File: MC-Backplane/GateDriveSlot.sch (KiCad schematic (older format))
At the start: 1 part, among them U6 86094328314755V1LF

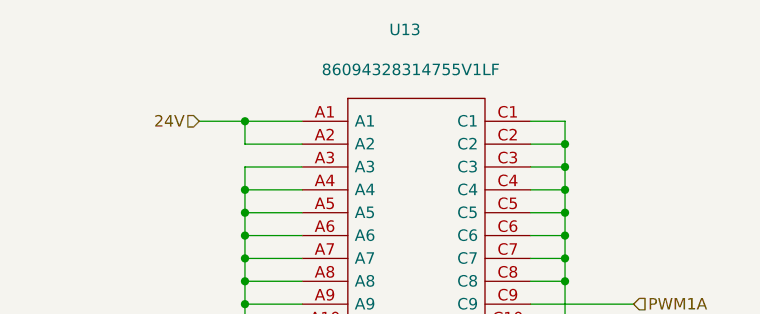
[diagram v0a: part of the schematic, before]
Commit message: placement done- tracks started
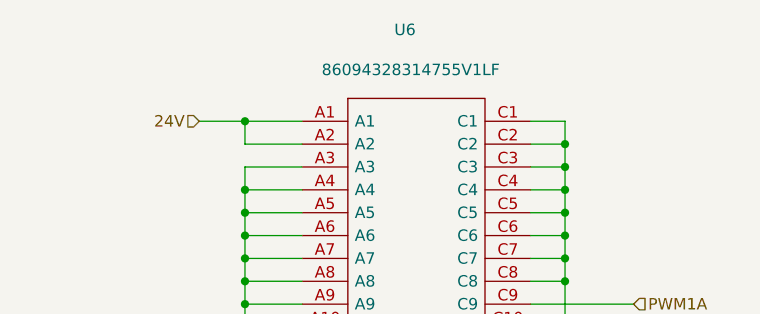
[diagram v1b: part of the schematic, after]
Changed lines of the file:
@@
 $Descr A4 11693 8268
 encoding utf-8
-Sheet 13 14
+Sheet 6 14
 Title ""
 Date ""
@@
 AR Path="/6245C75C/6229BF81" Ref="U8"  Part="1"
 AR Path="/6245C76A/6229BF81" Ref="U9"  Part="1"
-F 0 "U13" H 5375 2900 50  0000 C CNN
+F 0 "U6" H 5375 2900 50  0000 C CNN
 F 1 "86094328314755V1LF" H 5400 2725 50  0000 C CNN
 F 2 "Footprints_MC-Backplane:86094328314755V1LF" H 4925 2500 50  0001 C CNN

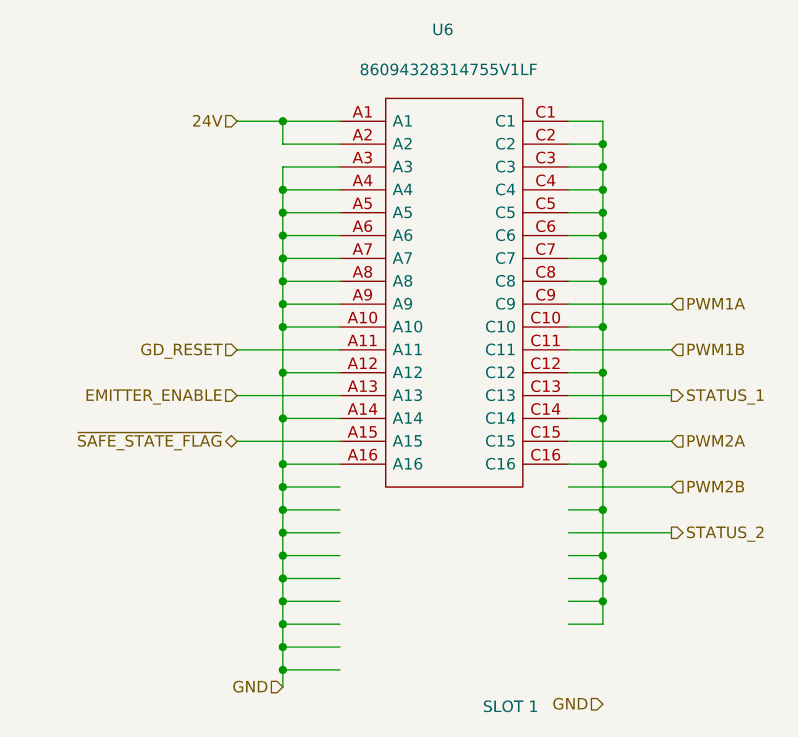
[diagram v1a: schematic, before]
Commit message: layout done: cleaning up and checking MH
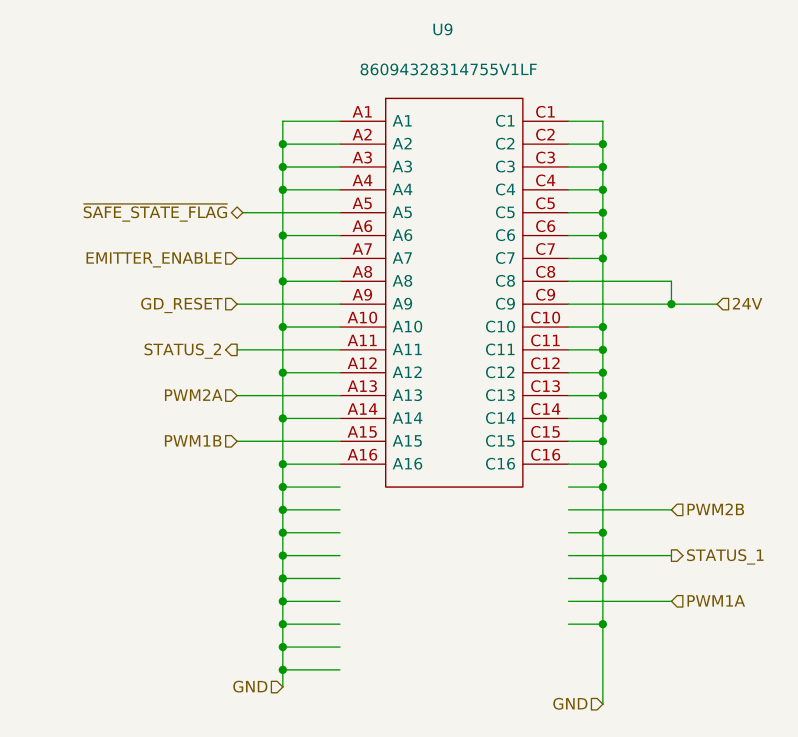
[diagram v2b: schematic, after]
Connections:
- wire segments 86 -> 87
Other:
- note removed: "SLOT 1"
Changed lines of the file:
@@
 $Descr A4 11693 8268
 encoding utf-8
-Sheet 6 14
+Sheet 9 14
 Title ""
 Date ""
@@
 AR Path="/6245C75C/6229BF81" Ref="U8"  Part="1"
 AR Path="/6245C76A/6229BF81" Ref="U9"  Part="1"
-F 0 "U6" H 5375 2900 50  0000 C CNN
+F 0 "U9" H 5375 2900 50  0000 C CNN
 F 1 "86094328314755V1LF" H 5400 2725 50  0000 C CNN
 F 2 "Footprints_MC-Backplane:86094328314755V1LF" H 4925 2500 50  0001 C CNN
@@
 $EndComp
 Wire Wire Line
-	5925 3300 6375 3300
-Wire Wire Line
 	5925 3400 6075 3400
-Wire Wire Line
-	6075 3400 6075 3600
-Wire Wire Line
-	6075 3400 6075 3200
-Wire Wire Line
-	6075 3200 5925 3200
 Connection ~ 6075 3400
 Wire Wire Line
-	5925 3600 6075 3600
-Connection ~ 6075 3600
-Wire Wire Line
-	6075 3600 6075 3800
-Wire Wire Line
-	5925 3800 6075 3800
-Connection ~ 6075 3800
-Wire Wire Line
-	6075 3800 6075 4000
-Wire Wire Line
-	5925 4000 6075 4000
-Connection ~ 6075 4000
-Wire Wire Line
-	6075 4000 6075 4200
-Wire Wire Line
-	5925 4200 6075 4200
-Connection ~ 6075 4200
-Wire Wire Line
-	6075 4200 6075 4400
-Wire Wire Line
-	5925 4400 6075 4400
-Connection ~ 6075 4400
-Wire Wire Line
-	6075 4400 6075 4500
-Wire Wire Line
-	5925 4600 6075 4600
-Wire Wire Line
-	4925 2700 4675 2700
-Wire Wire Line
-	4925 2900 4675 2900
-Connection ~ 4675 2900
-Wire Wire Line
-	4925 3100 4675 3100
-Connection ~ 4675 3100
-Wire Wire Line
-	4675 3100 4675 3200
+	4925 2500 4675 2500
 Wire Wire Line
 	4925 3200 4675 3200
 Connection ~ 4675 3200
 Wire Wire Line
-	4675 3200 4675 3300
-Wire Wire Line
-	4925 3300 4675 3300
-Connection ~ 4675 3300
-Wire Wire Line
-	4675 3300 4675 3400
-Wire Wire Line
 	4925 3400 4675 3400
-Text Notes 5550 5100 0    50   ~ 0
-SLOT 1
 Text HLabel 6075 5050 0    50   Input ~ 0
 GND
 Wire Wire Line
-	5925 3700 6375 3700
-Wire Wire Line
-	5925 3500 6375 3500
-Wire Wire Line
-	5925 4300 6375 4300
-Wire Wire Line
-	5925 3900 6375 3900
-Wire Wire Line
-	5925 4100 6375 4100
-Wire Wire Line
-	5925 4500 6075 4500
-Text HLabel 4475 2500 0    50   Input ~ 0
+	5925 4400 6375 4400
+Wire Wire Line
+	5925 4600 6375 4600
+Text HLabel 6575 3300 2    50   Input ~ 0
 24V
 Wire Wire Line
-	4675 2700 4675 2800
-Wire Wire Line
-	4675 2900 4675 3000
-Text HLabel 4475 3700 0    50   Input ~ 0
-EMITTER_ENABLE
-Wire Wire Line
-	4925 3900 4475 3900
-Wire Wire Line
-	4475 3700 4925 3700
-Wire Wire Line
-	4475 3500 4925 3500
+	4925 3700 4475 3700
+Wire Wire Line
+	5925 4200 6375 4200
+Wire Wire Line
+	4475 3900 4925 3900
 Wire Wire Line
 	4925 3600 4675 3600
-Wire Wire Line
-	4675 3600 4675 3800
-Wire Wire Line
-	4925 3800 4675 3800
-Connection ~ 4675 3800
 Wire Wire Line
 	4675 3400 4675 3600
 Connection ~ 4675 3400
-Connection ~ 4675 3600
-Connection ~ 6075 4500
-Wire Wire Line
-	6075 4500 6075 4600
-Wire Wire Line
-	4925 2800 4675 2800
-Connection ~ 4675 2800
-Wire Wire Line
-	4675 2800 4675 2900
+Wire Wire Line
+	4925 2600 4675 2600
 Wire Wire Line
 	4925 3000 4675 3000
 Connection ~ 4675 3000
 Wire Wire Line
-	4675 3000 4675 3100
-Wire Wire Line
-	4675 3800 4675 4000
-Wire Wire Line
-	4925 4000 4675 4000
-Connection ~ 4675 4000
-Wire Wire Line
-	4675 4000 4675 4100
-Wire Wire Line
-	4475 2500 4675 2500
-Wire Wire Line
-	4675 2600 4675 2500
-Wire Wire Line
-	4675 2600 4925 2600
-Connection ~ 4675 2500
-Wire Wire Line
-	4675 2500 4925 2500
-Wire Wire Line
-	5925 4700 6075 4700
+	6575 3300 6375 3300
+Wire Wire Line
+	6375 3200 6375 3300
+Wire Wire Line
+	6375 3200 5925 3200
+Connection ~ 6375 3300
+Wire Wire Line
+	6375 3300 5925 3300
 Wire Wire Line
 	4925 4100 4675 4100
-Connection ~ 4675 4100
 Wire Wire Line
 	4925 4200 4675 4200
@@
 Connection ~ 4675 4900
 Wire Wire Line
-	6075 3200 6075 3100
-Wire Wire Line
 	6075 2500 5925 2500
-Connection ~ 6075 3200
 Wire Wire Line
 	5925 2600 6075 2600
@@
 Wire Wire Line
 	6075 3100 6075 3000
-Text HLabel 4475 3900 0    50   BiDi ~ 0
+Text HLabel 6375 4600 2    50   Input ~ 0
+PWM1A
+Text HLabel 6375 4200 2    50   Input ~ 0
+PWM2B
+Text HLabel 4475 3700 0    50   Input ~ 0
+PWM2A
+Text HLabel 4475 3500 0    50   Output ~ 0
+STATUS_2
+Text HLabel 4475 3900 0    50   Input ~ 0
+PWM1B
+Text HLabel 6375 4400 2    50   Output ~ 0
+STATUS_1
+Text HLabel 4475 3300 0    50   Input ~ 0
+GD_RESET
+Text HLabel 4500 2900 0    50   BiDi ~ 0
 ~SAFE_STATE_FLAG~
-Text HLabel 4475 3500 0    50   Input ~ 0
-GD_RESET
-Text HLabel 6375 3700 2    50   Output ~ 0
-STATUS_1
-Text HLabel 6375 3500 2    50   Input ~ 0
-PWM1B
-Text HLabel 6375 4300 2    50   Output ~ 0
-STATUS_2
-Text HLabel 6375 3900 2    50   Input ~ 0
-PWM2A
-Text HLabel 6375 4100 2    50   Input ~ 0
-PWM2B
-Text HLabel 6375 3300 2    50   Input ~ 0
-PWM1A
-Wire Wire Line
-	6075 4600 6075 4700
-Connection ~ 6075 4600
+Text HLabel 4475 3100 0    50   Input ~ 0
+EMITTER_ENABLE
+Wire Wire Line
+	6075 3400 6075 3500
+Wire Wire Line
+	4925 2800 4675 2800
+Connection ~ 4675 2800
+Wire Wire Line
+	4675 3200 4675 3400
+Wire Wire Line
+	4475 3500 4925 3500
+Wire Wire Line
+	4675 3800 4675 4000
+Connection ~ 4675 4100
+Wire Wire Line
+	4675 3600 4675 3800
+Connection ~ 4675 3600
+Connection ~ 4675 3800
+Wire Wire Line
+	4675 3800 4925 3800
+Wire Wire Line
+	4675 2600 4675 2500
+Connection ~ 4675 2600
+Wire Wire Line
+	4675 2600 4675 2700
+Wire Wire Line
+	4925 3100 4475 3100
+Wire Wire Line
+	4925 3300 4475 3300
+Wire Wire Line
+	5925 3500 6075 3500
+Connection ~ 6075 3500
+Wire Wire Line
+	5925 3600 6075 3600
+Wire Wire Line
+	5925 3700 6075 3700
+Wire Wire Line
+	5925 3800 6075 3800
+Wire Wire Line
+	5925 3900 6075 3900
+Connection ~ 6075 3900
+Wire Wire Line
+	6075 3900 6075 4000
+Wire Wire Line
+	5925 4100 6075 4100
+Connection ~ 6075 4100
+Wire Wire Line
+	6075 4100 6075 4300
+Wire Wire Line
+	5925 4300 6075 4300
+Connection ~ 6075 4300
+Wire Wire Line
+	5925 4500 6075 4500
+Wire Wire Line
+	6075 4300 6075 4500
+Connection ~ 6075 4500
+Wire Wire Line
+	5925 4700 6075 4700
+Connection ~ 6075 4700
+Wire Wire Line
+	6075 4700 6075 5050
+Wire Wire Line
+	6075 3500 6075 3600
+Connection ~ 6075 3600
+Wire Wire Line
+	6075 3600 6075 3700
+Connection ~ 6075 3700
+Wire Wire Line
+	6075 3700 6075 3800
+Connection ~ 6075 3800
+Wire Wire Line
+	6075 3800 6075 3900
+Wire Wire Line
+	4675 3000 4675 3200
+Wire Wire Line
+	4675 2800 4675 3000
+Wire Wire Line
+	4925 2900 4500 2900
+Wire Wire Line
+	4925 2700 4675 2700
+Connection ~ 4675 2700
+Wire Wire Line
+	4675 2700 4675 2800
+Wire Wire Line
+	6075 3100 6075 3400
+Wire Wire Line
+	6075 4500 6075 4700
+Wire Wire Line
+	5925 4000 6075 4000
+Connection ~ 6075 4000
+Wire Wire Line
+	6075 4000 6075 4100
+Wire Wire Line
+	4925 4000 4675 4000
+Connection ~ 4675 4000
+Wire Wire Line
+	4675 4000 4675 4100
 $EndSCHEMATC

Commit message: Layout ready for review
- double check measurements and connector placement
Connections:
- wire segments 87 -> 55
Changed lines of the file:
@@
 $Descr A4 11693 8268
 encoding utf-8
-Sheet 9 14
+Sheet 6 14
 Title ""
 Date ""
@@
 Comment4 ""
 $EndDescr
+Wire Wire Line
+	4925 2500 4675 2500
+Wire Wire Line
+	4925 3200 4675 3200
+Connection ~ 4675 3200
+Wire Wire Line
+	4925 3400 4675 3400
+Text HLabel 6075 4350 0    50   Input ~ 0
+GND
+Wire Wire Line
+	5925 3700 6375 3700
+Wire Wire Line
+	5925 3900 6375 3900
+Text HLabel 6575 2600 2    50   Input ~ 0
+24V
+Wire Wire Line
+	4925 3700 4475 3700
+Wire Wire Line
+	5925 3500 6375 3500
+Wire Wire Line
+	4475 3900 4925 3900
+Wire Wire Line
+	4925 3600 4675 3600
+Wire Wire Line
+	4675 3400 4675 3600
+Connection ~ 4675 3400
+Wire Wire Line
+	4925 2600 4675 2600
+Wire Wire Line
+	4925 3000 4675 3000
+Connection ~ 4675 3000
+Wire Wire Line
+	6575 2600 6375 2600
+Wire Wire Line
+	6375 2500 6375 2600
+Wire Wire Line
+	6375 2500 5925 2500
+Connection ~ 6375 2600
+Wire Wire Line
+	6375 2600 5925 2600
+Text HLabel 4675 4350 0    50   Input ~ 0
+GND
+Text HLabel 6375 3900 2    50   Input ~ 0
+PWM1A
+Text HLabel 6375 3500 2    50   Input ~ 0
+PWM2B
+Text HLabel 4475 3700 0    50   Input ~ 0
+PWM2A
+Text HLabel 4475 3500 0    50   Output ~ 0
+STATUS_2
+Text HLabel 4475 3900 0    50   Input ~ 0
+PWM1B
+Text HLabel 6375 3700 2    50   Output ~ 0
+STATUS_1
+Text HLabel 4475 3300 0    50   Input ~ 0
+GD_RESET
+Text HLabel 4500 2900 0    50   BiDi ~ 0
+~SAFE_STATE_FLAG~
+Text HLabel 4475 3100 0    50   Input ~ 0
+EMITTER_ENABLE
+Wire Wire Line
+	4925 2800 4675 2800
+Connection ~ 4675 2800
+Wire Wire Line
+	4675 3200 4675 3400
+Wire Wire Line
+	4475 3500 4925 3500
+Wire Wire Line
+	4675 3800 4675 4000
+Wire Wire Line
+	4675 3600 4675 3800
+Connection ~ 4675 3600
+Connection ~ 4675 3800
+Wire Wire Line
+	4675 3800 4925 3800
+Wire Wire Line
+	4675 2600 4675 2500
+Connection ~ 4675 2600
+Wire Wire Line
+	4675 2600 4675 2700
+Wire Wire Line
+	4925 3100 4475 3100
+Wire Wire Line
+	4925 3300 4475 3300
+Wire Wire Line
+	5925 3400 6075 3400
+Wire Wire Line
+	6075 3400 6075 3600
+Wire Wire Line
+	5925 3600 6075 3600
+Connection ~ 6075 3600
+Wire Wire Line
+	5925 3800 6075 3800
+Wire Wire Line
+	6075 3600 6075 3800
+Connection ~ 6075 3800
+Wire Wire Line
+	5925 4000 6075 4000
+Connection ~ 6075 4000
+Wire Wire Line
+	6075 4000 6075 4350
+Wire Wire Line
+	4675 3000 4675 3200
+Wire Wire Line
+	4675 2800 4675 3000
+Wire Wire Line
+	4925 2900 4500 2900
+Wire Wire Line
+	4925 2700 4675 2700
+Connection ~ 4675 2700
+Wire Wire Line
+	4675 2700 4675 2800
+Wire Wire Line
+	6075 3800 6075 4000
+Wire Wire Line
+	4925 4000 4675 4000
+Connection ~ 6075 3400
+Wire Wire Line
+	6075 3300 6075 3400
+Connection ~ 6075 3300
+Wire Wire Line
+	5925 3300 6075 3300
+Wire Wire Line
+	6075 3200 6075 3300
+Connection ~ 6075 3200
+Wire Wire Line
+	5925 3200 6075 3200
+Wire Wire Line
+	6075 3100 6075 3200
+Connection ~ 6075 3100
+Wire Wire Line
+	5925 3100 6075 3100
+Wire Wire Line
+	6075 3000 6075 3100
+Connection ~ 6075 3000
+Wire Wire Line
+	5925 3000 6075 3000
+Wire Wire Line
+	6075 2900 6075 3000
+Connection ~ 6075 2900
+Wire Wire Line
+	5925 2900 6075 2900
+Wire Wire Line
+	6075 2800 6075 2900
+Connection ~ 6075 2800
+Wire Wire Line
+	5925 2800 6075 2800
+Wire Wire Line
+	6075 2700 6075 2800
+Wire Wire Line
+	5925 2700 6075 2700
+Connection ~ 4675 4000
 $Comp
 L Existing_IC_Models:86094328314755V1LF U?
@@
 AR Path="/6245C75C/6229BF81" Ref="U8"  Part="1"
 AR Path="/6245C76A/6229BF81" Ref="U9"  Part="1"
-F 0 "U9" H 5375 2900 50  0000 C CNN
+F 0 "U6" H 5375 2900 50  0000 C CNN
 F 1 "86094328314755V1LF" H 5400 2725 50  0000 C CNN
 F 2 "Footprints_MC-Backplane:86094328314755V1LF" H 4925 2500 50  0001 C CNN
@@
 $EndComp
 Wire Wire Line
-	5925 3400 6075 3400
-Connection ~ 6075 3400
-Wire Wire Line
-	4925 2500 4675 2500
-Wire Wire Line
-	4925 3200 4675 3200
-Connection ~ 4675 3200
-Wire Wire Line
-	4925 3400 4675 3400
-Text HLabel 6075 5050 0    50   Input ~ 0
-GND
-Wire Wire Line
-	5925 4400 6375 4400
-Wire Wire Line
-	5925 4600 6375 4600
-Text HLabel 6575 3300 2    50   Input ~ 0
-24V
-Wire Wire Line
-	4925 3700 4475 3700
-Wire Wire Line
-	5925 4200 6375 4200
-Wire Wire Line
-	4475 3900 4925 3900
-Wire Wire Line
-	4925 3600 4675 3600
-Wire Wire Line
-	4675 3400 4675 3600
-Connection ~ 4675 3400
-Wire Wire Line
-	4925 2600 4675 2600
-Wire Wire Line
-	4925 3000 4675 3000
-Connection ~ 4675 3000
-Wire Wire Line
-	6575 3300 6375 3300
-Wire Wire Line
-	6375 3200 6375 3300
-Wire Wire Line
-	6375 3200 5925 3200
-Connection ~ 6375 3300
-Wire Wire Line
-	6375 3300 5925 3300
-Wire Wire Line
-	4925 4100 4675 4100
-Wire Wire Line
-	4925 4200 4675 4200
-Wire Wire Line
-	4925 4300 4675 4300
-Wire Wire Line
-	4925 4400 4675 4400
-Wire Wire Line
-	4925 4500 4675 4500
-Wire Wire Line
-	4925 4600 4675 4600
-Wire Wire Line
-	4925 4700 4675 4700
-Wire Wire Line
-	4925 4800 4675 4800
-Wire Wire Line
-	4925 4900 4675 4900
-Connection ~ 4675 4400
-Wire Wire Line
-	4675 4400 4675 4500
-Connection ~ 4675 4500
-Wire Wire Line
-	4675 4500 4675 4600
-Connection ~ 4675 4600
-Wire Wire Line
-	4675 4600 4675 4700
-Connection ~ 4675 4700
-Wire Wire Line
-	4675 4700 4675 4800
-Connection ~ 4675 4800
-Wire Wire Line
-	4675 4800 4675 4900
-Text HLabel 4675 4975 0    50   Input ~ 0
-GND
-Wire Wire Line
-	4675 4100 4675 4200
-Connection ~ 4675 4300
-Wire Wire Line
-	4675 4300 4675 4400
-Connection ~ 4675 4200
-Wire Wire Line
-	4675 4200 4675 4300
-Wire Wire Line
-	4675 4900 4675 4975
-Connection ~ 4675 4900
-Wire Wire Line
-	6075 2500 5925 2500
-Wire Wire Line
-	5925 2600 6075 2600
-Connection ~ 6075 2600
-Wire Wire Line
-	6075 2600 6075 2500
-Wire Wire Line
-	5925 2700 6075 2700
-Connection ~ 6075 2700
-Wire Wire Line
-	6075 2700 6075 2600
-Wire Wire Line
-	5925 2800 6075 2800
-Connection ~ 6075 2800
-Wire Wire Line
-	6075 2800 6075 2700
-Wire Wire Line
-	5925 2900 6075 2900
-Connection ~ 6075 2900
-Wire Wire Line
-	6075 2900 6075 2800
-Wire Wire Line
-	5925 3000 6075 3000
-Connection ~ 6075 3000
-Wire Wire Line
-	6075 3000 6075 2900
-Wire Wire Line
-	5925 3100 6075 3100
-Connection ~ 6075 3100
-Wire Wire Line
-	6075 3100 6075 3000
-Text HLabel 6375 4600 2    50   Input ~ 0
-PWM1A
-Text HLabel 6375 4200 2    50   Input ~ 0
-PWM2B
-Text HLabel 4475 3700 0    50   Input ~ 0
-PWM2A
-Text HLabel 4475 3500 0    50   Output ~ 0
-STATUS_2
-Text HLabel 4475 3900 0    50   Input ~ 0
-PWM1B
-Text HLabel 6375 4400 2    50   Output ~ 0
-STATUS_1
-Text HLabel 4475 3300 0    50   Input ~ 0
-GD_RESET
-Text HLabel 4500 2900 0    50   BiDi ~ 0
-~SAFE_STATE_FLAG~
-Text HLabel 4475 3100 0    50   Input ~ 0
-EMITTER_ENABLE
-Wire Wire Line
-	6075 3400 6075 3500
-Wire Wire Line
-	4925 2800 4675 2800
-Connection ~ 4675 2800
-Wire Wire Line
-	4675 3200 4675 3400
-Wire Wire Line
-	4475 3500 4925 3500
-Wire Wire Line
-	4675 3800 4675 4000
-Connection ~ 4675 4100
-Wire Wire Line
-	4675 3600 4675 3800
-Connection ~ 4675 3600
-Connection ~ 4675 3800
-Wire Wire Line
-	4675 3800 4925 3800
-Wire Wire Line
-	4675 2600 4675 2500
-Connection ~ 4675 2600
-Wire Wire Line
-	4675 2600 4675 2700
-Wire Wire Line
-	4925 3100 4475 3100
-Wire Wire Line
-	4925 3300 4475 3300
-Wire Wire Line
-	5925 3500 6075 3500
-Connection ~ 6075 3500
-Wire Wire Line
-	5925 3600 6075 3600
-Wire Wire Line
-	5925 3700 6075 3700
-Wire Wire Line
-	5925 3800 6075 3800
-Wire Wire Line
-	5925 3900 6075 3900
-Connection ~ 6075 3900
-Wire Wire Line
-	6075 3900 6075 4000
-Wire Wire Line
-	5925 4100 6075 4100
-Connection ~ 6075 4100
-Wire Wire Line
-	6075 4100 6075 4300
-Wire Wire Line
-	5925 4300 6075 4300
-Connection ~ 6075 4300
-Wire Wire Line
-	5925 4500 6075 4500
-Wire Wire Line
-	6075 4300 6075 4500
-Connection ~ 6075 4500
-Wire Wire Line
-	5925 4700 6075 4700
-Connection ~ 6075 4700
-Wire Wire Line
-	6075 4700 6075 5050
-Wire Wire Line
-	6075 3500 6075 3600
-Connection ~ 6075 3600
-Wire Wire Line
-	6075 3600 6075 3700
-Connection ~ 6075 3700
-Wire Wire Line
-	6075 3700 6075 3800
-Connection ~ 6075 3800
-Wire Wire Line
-	6075 3800 6075 3900
-Wire Wire Line
-	4675 3000 4675 3200
-Wire Wire Line
-	4675 2800 4675 3000
-Wire Wire Line
-	4925 2900 4500 2900
-Wire Wire Line
-	4925 2700 4675 2700
-Connection ~ 4675 2700
-Wire Wire Line
-	4675 2700 4675 2800
-Wire Wire Line
-	6075 3100 6075 3400
-Wire Wire Line
-	6075 4500 6075 4700
-Wire Wire Line
-	5925 4000 6075 4000
-Connection ~ 6075 4000
-Wire Wire Line
-	6075 4000 6075 4100
-Wire Wire Line
-	4925 4000 4675 4000
-Connection ~ 4675 4000
-Wire Wire Line
-	4675 4000 4675 4100
+	4675 4000 4675 4350
 $EndSCHEMATC

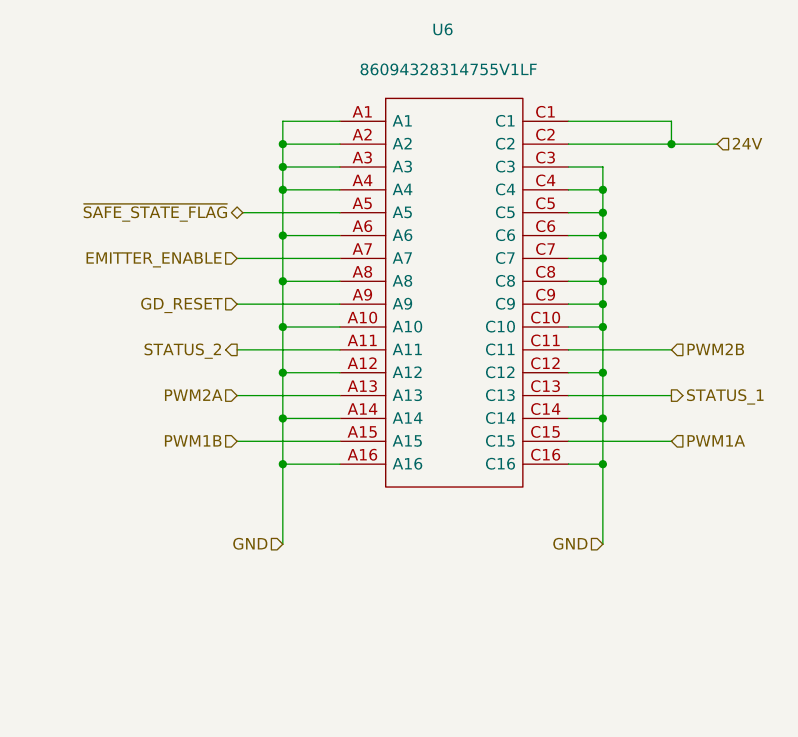
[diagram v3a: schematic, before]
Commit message: added testpoints
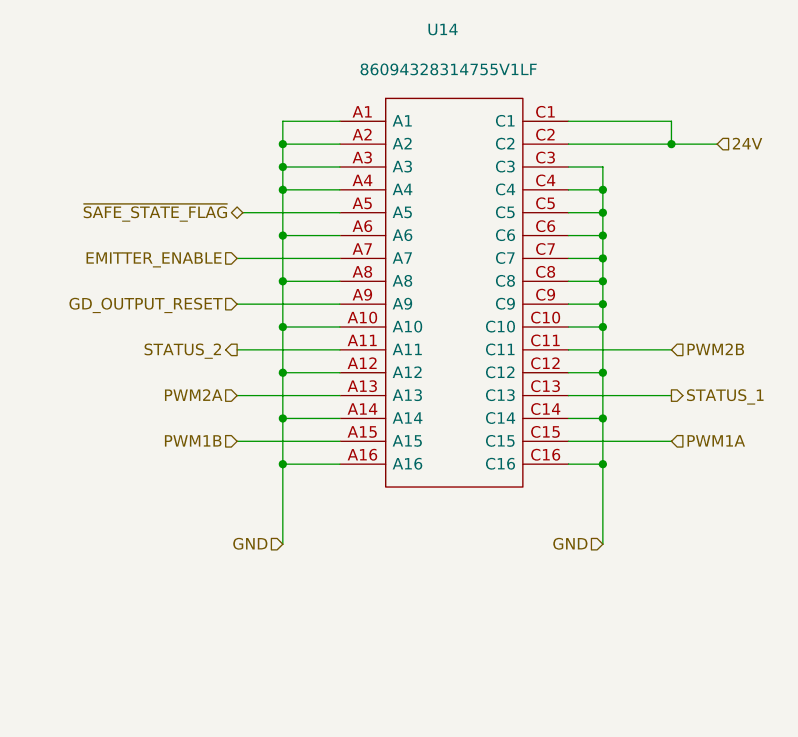
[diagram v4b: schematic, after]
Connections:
- net GD_RESET renamed GD_OUTPUT_RESET
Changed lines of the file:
@@
 STATUS_1
 Text HLabel 4475 3300 0    50   Input ~ 0
-GD_RESET
+GD_OUTPUT_RESET
 Text HLabel 4500 2900 0    50   BiDi ~ 0
 ~SAFE_STATE_FLAG~
@@
 AR Path="/6245C75C/6229BF81" Ref="U8"  Part="1"
 AR Path="/6245C76A/6229BF81" Ref="U9"  Part="1"
-F 0 "U6" H 5375 2900 50  0000 C CNN
+F 0 "U14" H 5375 2900 50  0000 C CNN
 F 1 "86094328314755V1LF" H 5400 2725 50  0000 C CNN
 F 2 "Footprints_MC-Backplane:86094328314755V1LF" H 4925 2500 50  0001 C CNN
